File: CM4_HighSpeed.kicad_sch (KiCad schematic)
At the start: 8 parts, among them J6 Conn_01x22_Female, J7 Conn_01x22_Female, U6 RT9742SNGV

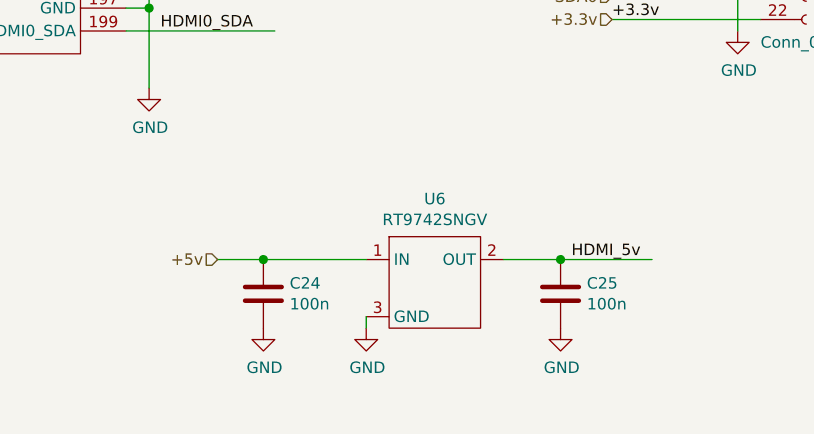
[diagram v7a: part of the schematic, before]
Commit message: additional layout, power circuitry
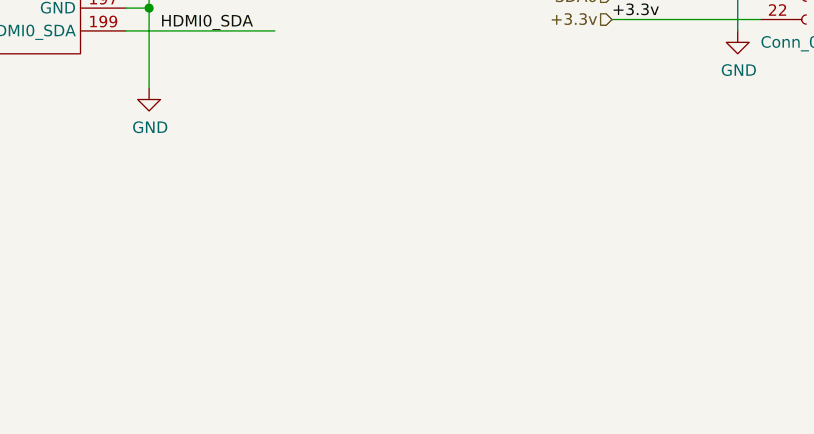
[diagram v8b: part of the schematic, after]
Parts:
- removed C24, C25: 100n, Capacitor_SMD:C_0402_1005Metric, symbol Device:C
- removed U6: RT9742SNGV, Package_TO_SOT_SMD:SOT-23, symbol CM4IO:RT9742SNGV
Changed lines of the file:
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@@
   (junction (at 105.41 140.97) (diameter 1.016) (color 0 0 0 0))
   (junction (at 105.41 148.59) (diameter 1.016) (color 0 0 0 0))
-  (junction (at 118.11 176.53) (diameter 1.016) (color 0 0 0 0))
-  (junction (at 151.13 176.53) (diameter 1.016) (color 0 0 0 0))
   (junction (at 170.815 36.83) (diameter 1.016) (color 0 0 0 0))
   (junction (at 170.815 44.45) (diameter 1.016) (color 0 0 0 0))
@@
   (junction (at 170.815 134.62) (diameter 1.016) (color 0 0 0 0))
   (junction (at 170.815 142.24) (diameter 1.016) (color 0 0 0 0))
+  (no_connect (at 41.91 31.75))
+  (no_connect (at 173.355 62.23))
+  (no_connect (at 173.355 64.77))
+  (no_connect (at 173.355 72.39))
+  (no_connect (at 173.355 139.7))
   (no_connect (at 173.355 57.15))
+  (no_connect (at 41.91 29.21))
   (no_connect (at 173.355 54.61))
-  (no_connect (at 41.91 29.21))
-  (no_connect (at 173.355 64.77))
-  (no_connect (at 173.355 62.23))
-  (no_connect (at 173.355 139.7))
-  (no_connect (at 41.91 31.75))
-  (no_connect (at 173.355 72.39))
   (wire (pts (xy 25.4 74.93) (xy 41.91 74.93))
     (stroke (width 0) (type solid) (color 0 0 0 0))
@@
     (stroke (width 0) (type solid) (color 0 0 0 0))
   )
-  (wire (pts (xy 113.03 176.53) (xy 118.11 176.53))
-    (stroke (width 0) (type solid) (color 0 0 0 0))
-  )
-  (wire (pts (xy 118.11 176.53) (xy 129.54 176.53))
-    (stroke (width 0) (type solid) (color 0 0 0 0))
-  )
   (wire (pts (xy 119.38 44.45) (xy 102.87 44.45))
     (stroke (width 0) (type solid) (color 0 0 0 0))
@@
   )
   (wire (pts (xy 119.38 130.81) (xy 102.87 130.81))
-    (stroke (width 0) (type solid) (color 0 0 0 0))
-  )
-  (wire (pts (xy 129.54 182.88) (xy 129.54 184.15))
-    (stroke (width 0) (type solid) (color 0 0 0 0))
-  )
-  (wire (pts (xy 144.78 176.53) (xy 151.13 176.53))
-    (stroke (width 0) (type solid) (color 0 0 0 0))
-  )
-  (wire (pts (xy 151.13 176.53) (xy 161.29 176.53))
     (stroke (width 0) (type solid) (color 0 0 0 0))
   )
@@
     (effects (font (size 1.27 1.27)) (justify left bottom))
   )
-  (label "HDMI_5v" (at 160.02 176.53 180)
-    (effects (font (size 1.27 1.27)) (justify right bottom))
-  )
   (label "SCL1" (at 161.925 77.47 180)
     (effects (font (size 1.27 1.27)) (justify right bottom))
@@
   (hierarchical_label "TV_OUT" (shape output) (at 109.22 39.37 0)
     (effects (font (size 1.27 1.27)) (justify left))
-  )
-  (hierarchical_label "+5v" (shape input) (at 113.03 176.53 180)
-    (effects (font (size 1.27 1.27)) (justify right))
   )
   (hierarchical_label "CAM_GPIO" (shape input) (at 156.845 69.85 180)
@@
     )
   )
-  (symbol (lib_id "power:GND") (at 118.11 184.15 0) (unit 1)
-    (in_bom yes) (on_board yes)
-    (property "Reference" "#PWR024" (id 0) (at 118.11 190.5 0)
-      (effects (font (size 1.27 1.27)) hide)
-    )
-    (property "Value" "GND" (id 1) (at 118.237 188.5442 0))
-    (property "Footprint" "" (id 2) (at 118.11 184.15 0)
-      (effects (font (size 1.27 1.27)) hide)
-    )
-    (property "Datasheet" "" (id 3) (at 118.11 184.15 0)
-      (effects (font (size 1.27 1.27)) hide)
-    )
-  )
-  (symbol (lib_id "power:GND") (at 129.54 184.15 0) (unit 1)
-    (in_bom yes) (on_board yes)
-    (property "Reference" "#PWR025" (id 0) (at 129.54 190.5 0)
-      (effects (font (size 1.27 1.27)) hide)
-    )
-    (property "Value" "GND" (id 1) (at 129.667 188.5442 0))
-    (property "Footprint" "" (id 2) (at 129.54 184.15 0)
-      (effects (font (size 1.27 1.27)) hide)
-    )
-    (property "Datasheet" "" (id 3) (at 129.54 184.15 0)
-      (effects (font (size 1.27 1.27)) hide)
-    )
-  )
-  (symbol (lib_id "power:GND") (at 151.13 184.15 0) (unit 1)
-    (in_bom yes) (on_board yes)
-    (property "Reference" "#PWR026" (id 0) (at 151.13 190.5 0)
-      (effects (font (size 1.27 1.27)) hide)
-    )
-    (property "Value" "GND" (id 1) (at 151.257 188.5442 0))
-    (property "Footprint" "" (id 2) (at 151.13 184.15 0)
-      (effects (font (size 1.27 1.27)) hide)
-    )
-    (property "Datasheet" "" (id 3) (at 151.13 184.15 0)
-      (effects (font (size 1.27 1.27)) hide)
-    )
-  )
   (symbol (lib_id "power:GND") (at 170.815 83.82 0) (unit 1)
     (in_bom yes) (on_board yes)
-    (property "Reference" "#PWR027" (id 0) (at 170.815 90.17 0)
+    (property "Reference" "#PWR024" (id 0) (at 170.815 90.17 0)
       (effects (font (size 1.27 1.27)) hide)
     )
@@
   (symbol (lib_id "power:GND") (at 170.815 151.13 0) (unit 1)
     (in_bom yes) (on_board yes)
-    (property "Reference" "#PWR028" (id 0) (at 170.815 157.48 0)
+    (property "Reference" "#PWR025" (id 0) (at 170.815 157.48 0)
       (effects (font (size 1.27 1.27)) hide)
     )
@@
       (effects (font (size 1.27 1.27)) hide)
     )
-  )
-  (symbol (lib_id "Device:C") (at 118.11 180.34 0) (unit 1)
-    (in_bom yes) (on_board yes)
-    (property "Reference" "C24" (id 0) (at 121.031 179.1716 0)
-      (effects (font (size 1.27 1.27)) (justify left))
-    )
-    (property "Value" "100n" (id 1) (at 121.031 181.483 0)
-      (effects (font (size 1.27 1.27)) (justify left))
-    )
-    (property "Footprint" "Capacitor_SMD:C_0402_1005Metric" (id 2) (at 119.0752 184.15 0)
-      (effects (font (size 1.27 1.27)) hide)
-    )
-    (property "Datasheet" "https://search.murata.co.jp/Ceramy/image/img/A01X/G101/ENG/GRM155R71C104KA88-01.pdf" (id 3) (at 118.11 180.34 0)
-      (effects (font (size 1.27 1.27)) hide)
-    )
-    (property "Field4" "Farnell" (id 4) (at 118.11 180.34 0)
-      (effects (font (size 1.27 1.27)) hide)
-    )
-    (property "Field5" "2611911" (id 5) (at 118.11 180.34 0)
-      (effects (font (size 1.27 1.27)) hide)
-    )
-    (property "Field6" "RM EMK105 B7104KV-F" (id 6) (at 118.11 180.34 0)
-      (effects (font (size 1.27 1.27)) hide)
-    )
-    (property "Field7" "TAIYO YUDEN EUROPE GMBH" (id 7) (at 118.11 180.34 0)
-      (effects (font (size 1.27 1.27)) hide)
-    )
-    (property "Part Description" "	0.1uF 10% 16V Ceramic Capacitor X7R 0402 (1005 Metric)" (id 8) (at 118.11 180.34 0)
-      (effects (font (size 1.27 1.27)) hide)
-    )
-    (property "Field8" "110091611" (id 9) (at 118.11 180.34 0)
-      (effects (font (size 1.27 1.27)) hide)
-    )
-  )
-  (symbol (lib_id "Device:C") (at 151.13 180.34 0) (unit 1)
-    (in_bom yes) (on_board yes)
-    (property "Reference" "C25" (id 0) (at 154.051 179.1716 0)
-      (effects (font (size 1.27 1.27)) (justify left))
-    )
-    (property "Value" "100n" (id 1) (at 154.051 181.483 0)
-      (effects (font (size 1.27 1.27)) (justify left))
-    )
-    (property "Footprint" "Capacitor_SMD:C_0402_1005Metric" (id 2) (at 152.0952 184.15 0)
-      (effects (font (size 1.27 1.27)) hide)
-    )
-    (property "Datasheet" "https://search.murata.co.jp/Ceramy/image/img/A01X/G101/ENG/GRM155R71C104KA88-01.pdf" (id 3) (at 151.13 180.34 0)
-      (effects (font (size 1.27 1.27)) hide)
-    )
-    (property "Field4" "Farnell" (id 4) (at 151.13 180.34 0)
-      (effects (font (size 1.27 1.27)) hide)
-    )
-    (property "Field5" "2611911" (id 5) (at 151.13 180.34 0)
-      (effects (font (size 1.27 1.27)) hide)
-    )
-    (property "Field6" "RM EMK105 B7104KV-F" (id 6) (at 151.13 180.34 0)
-      (effects (font (size 1.27 1.27)) hide)
-    )
-    (property "Field7" "TAIYO YUDEN EUROPE GMBH" (id 7) (at 151.13 180.34 0)
-      (effects (font (size 1.27 1.27)) hide)
-    )
-    (property "Part Description" "	0.1uF 10% 16V Ceramic Capacitor X7R 0402 (1005 Metric)" (id 8) (at 151.13 180.34 0)
-      (effects (font (size 1.27 1.27)) hide)
-    )
-    (property "Field8" "110091611" (id 9) (at 151.13 180.34 0)
-      (effects (font (size 1.27 1.27)) hide)
-    )
-  )
-  (symbol (lib_id "CM4IO:RT9742SNGV") (at 134.62 180.34 0) (unit 1)
-    (in_bom yes) (on_board yes)
-    (property "Reference" "U6" (id 0) (at 137.16 169.799 0))
-    (property "Value" "RT9742SNGV" (id 1) (at 137.16 172.1104 0))
-    (property "Footprint" "Package_TO_SOT_SMD:SOT-23" (id 2) (at 134.62 180.34 0)
-      (effects (font (size 1.27 1.27)) hide)
-    )
-    (property "Datasheet" "https://www.richtek.com/assets/product_file/RT9742/DS9742-09.pdf" (id 3) (at 134.62 180.34 0)
-      (effects (font (size 1.27 1.27)) hide)
-    )
-    (property "Field4" "Farnell" (id 4) (at 134.62 180.34 0)
-      (effects (font (size 1.27 1.27)) hide)
-    )
-    (property "Field5" "2575555" (id 5) (at 134.62 180.34 0)
-      (effects (font (size 1.27 1.27)) hide)
-    )
-    (property "Field6" "RT9742SNGV" (id 6) (at 134.62 180.34 0)
-      (effects (font (size 1.27 1.27)) hide)
-    )
-    (property "Field7" "RichTek" (id 7) (at 134.62 180.34 0)
-      (effects (font (size 1.27 1.27)) hide)
-    )
-    (property "Part Description" "Power Switch/Driver 1:1 N-Channel 500mA SOT-23-3" (id 8) (at 134.62 180.34 0)
-      (effects (font (size 1.27 1.27)) hide)
-    )
-    (property "Field8" "USWI00155" (id 9) (at 134.62 180.34 0)
-      (effects (font (size 1.27 1.27)) hide)
-    )
